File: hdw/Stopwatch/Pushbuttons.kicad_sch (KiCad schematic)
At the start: 42 parts

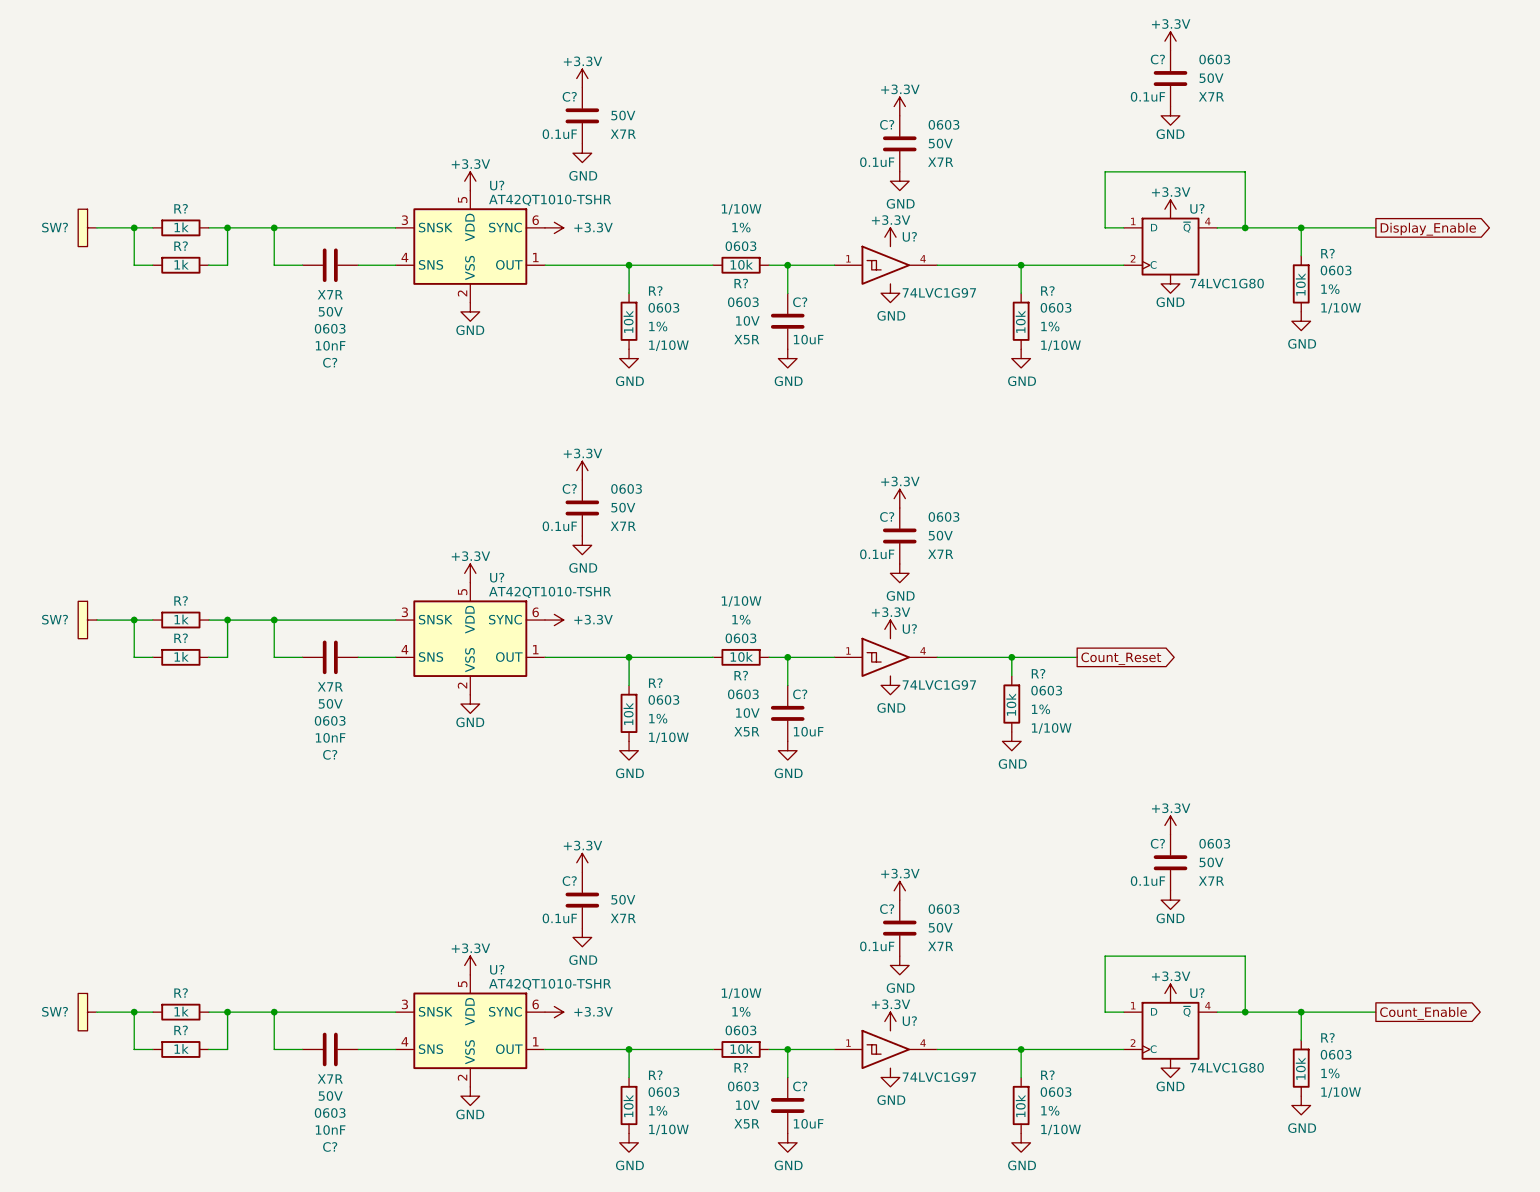
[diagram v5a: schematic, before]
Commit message: Assigned some digikey pns
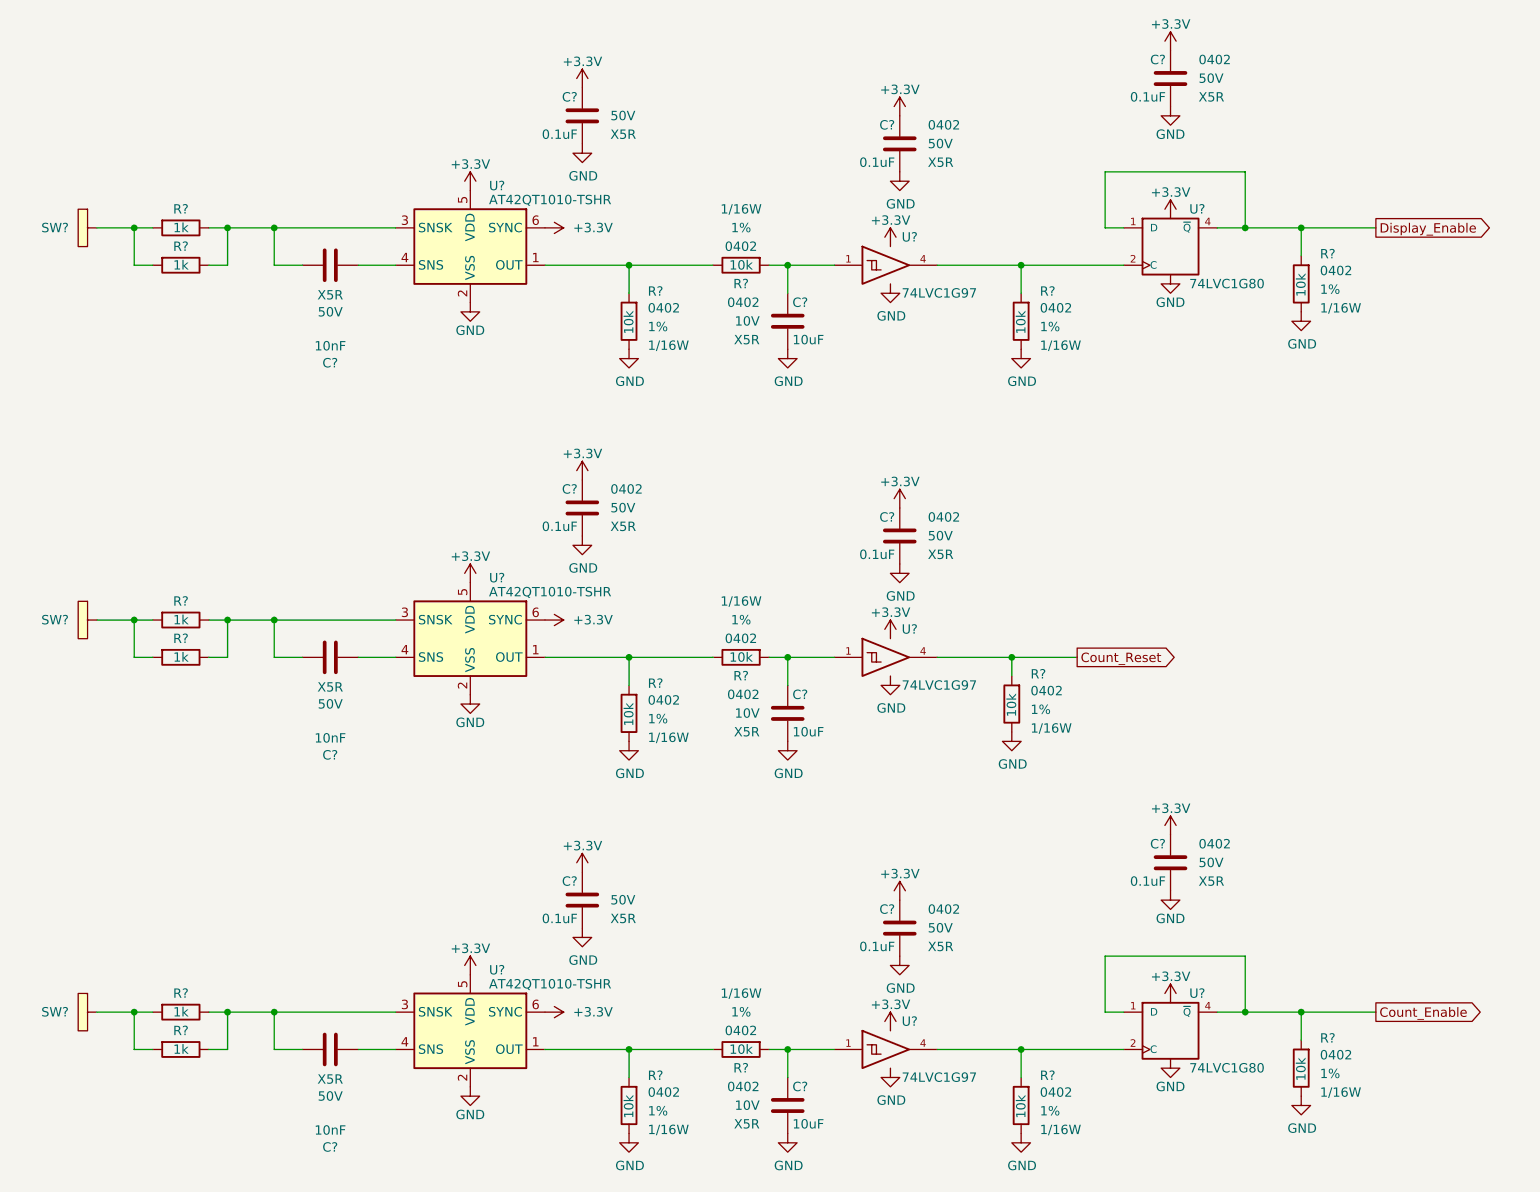
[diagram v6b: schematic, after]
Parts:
- C? (x3): footprint Capacitors_SMD:C_0603 -> Capacitors_SMD:C_0402; Dielectric X7R -> X5R; Digi-Key PN 1276-1921-1-ND -> 445-12201-1-ND; display_footprint 0603 -> (none)
- C? (x8): footprint Capacitors_SMD:C_0603 -> Capacitors_SMD:C_0402; Dielectric X7R -> X5R; Digi-Key PN 311-1344-1-ND -> 490-10697-1-ND; display_footprint 0603 -> 0402
- C? (x3): footprint Capacitors_SMD:C_0603 -> Capacitors_SMD:C_0402; Digi-Key PN 490-14372-1-ND -> 490-GRM155R61A106ME11DCT-ND; display_footprint 0603 -> 0402
- R? (x11): footprint Resistors_SMD:R_0603 -> Resistors_SMD:R_0402; Digi-Key PN RMCF0603FT10K0CT-ND -> RMCF0402FT10K0CT-ND; Wattage 1/10W -> 1/16W; display_footprint 0603 -> 0402
- R? (x6): footprint Resistors_SMD:R_0603 -> Resistors_SMD:R_0402; Digi-Key PN RHM1.0KDCT-ND -> RMCF0402FT1K00CT-ND; Wattage 1/10W -> 1/16W; display_footprint 0603 -> 0402
- U? (x2): footprint TO_SOT_Packages_SMD:SOT-353_SC-70-5 -> Package_SON:Texas_X2SON-5_0.8x0.8mm_P0.48mm; Digi-Key PN 296-9852-1-ND -> 1727-74LVC1G80GX,125CT-ND
- U? (x3): footprint Package_TO_SOT_SMD:SOT-363_SC-70-6 -> (none); Digi-Key PN (none) -> 296-29875-1-ND

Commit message: added proper power sequencing, discharge
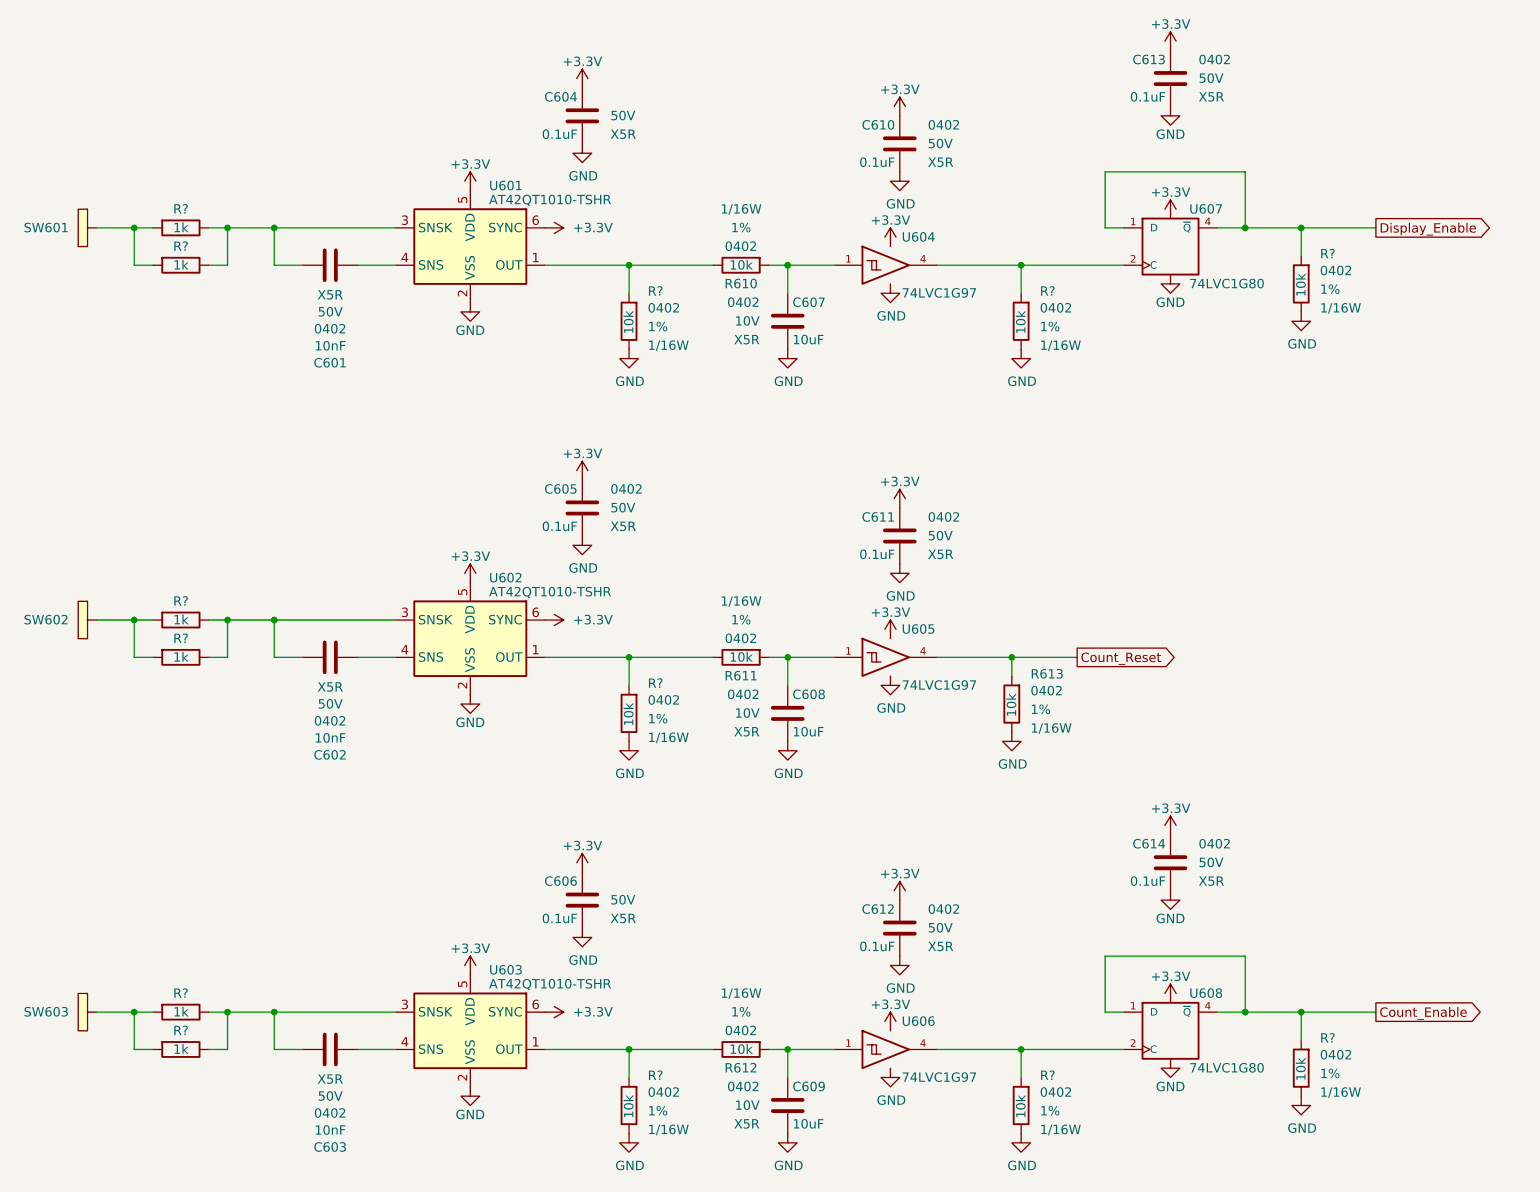
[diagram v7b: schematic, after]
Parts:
- C601, C602, C603: renamed from C?; display_footprint (none) -> 0402
- U604, U605, U606: renamed from U?; footprint (none) -> Package_SON:Fairchild_MicroPak2-6_1.0x1.0mm_P0.35mm
- gave numbers to parts that had none: 23

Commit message: lots and lots of routing
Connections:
- net +3V3 renamed +3.3V
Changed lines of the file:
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@@
     )
   )
-  (symbol (lib_id "Incrementor-rescue:+3.3V-power") (at 194.31 40.64 0) (unit 1)
+  (symbol (lib_id "power:+3.3V") (at 194.31 40.64 0) (unit 1)
     (in_bom yes) (on_board yes) (dnp no)
     (property "Reference" "#PWR0639" (at 194.31 44.45 0)
@@
     )
   )
-  (symbol (lib_id "Incrementor-rescue:+3.3V-power") (at 194.31 17.78 0) (unit 1)
+  (symbol (lib_id "power:+3.3V") (at 194.31 17.78 0) (unit 1)
     (in_bom yes) (on_board yes) (dnp no)
     (property "Reference" "#PWR0637" (at 194.31 21.59 0)
@@
     )
   )
-  (symbol (lib_id "Incrementor-rescue:+3.3V-power") (at 156.21 44.45 0) (unit 1)
+  (symbol (lib_id "power:+3.3V") (at 156.21 44.45 0) (unit 1)
     (in_bom yes) (on_board yes) (dnp no)
     (property "Reference" "#PWR0622" (at 156.21 48.26 0)
@@
     )
   )
-  (symbol (lib_id "Incrementor-rescue:+3.3V-power") (at 157.48 26.67 0) (unit 1)
+  (symbol (lib_id "power:+3.3V") (at 157.48 26.67 0) (unit 1)
     (in_bom yes) (on_board yes) (dnp no)
     (property "Reference" "#PWR0628" (at 157.48 30.48 0)
@@
     )
   )
-  (symbol (lib_id "Incrementor-rescue:+3.3V-power") (at 156.21 97.79 0) (unit 1)
+  (symbol (lib_id "power:+3.3V") (at 156.21 97.79 0) (unit 1)
     (in_bom yes) (on_board yes) (dnp no)
     (property "Reference" "#PWR0624" (at 156.21 101.6 0)
@@
     )
   )
-  (symbol (lib_id "Incrementor-rescue:+3.3V-power") (at 157.48 80.01 0) (unit 1)
+  (symbol (lib_id "power:+3.3V") (at 157.48 80.01 0) (unit 1)
     (in_bom yes) (on_board yes) (dnp no)
     (property "Reference" "#PWR0630" (at 157.48 83.82 0)
@@
     )
   )
-  (symbol (lib_id "Incrementor-rescue:+3.3V-power") (at 114.3 76.2 0) (unit 1)
+  (symbol (lib_id "power:+3.3V") (at 114.3 76.2 0) (unit 1)
     (in_bom yes) (on_board yes) (dnp no)
     (property "Reference" "#PWR0612" (at 114.3 80.01 0)
@@
     )
   )
-  (symbol (lib_id "Incrementor-rescue:+3.3V-power") (at 157.48 133.35 0) (unit 1)
+  (symbol (lib_id "power:+3.3V") (at 157.48 133.35 0) (unit 1)
     (in_bom yes) (on_board yes) (dnp no)
     (property "Reference" "#PWR0632" (at 157.48 137.16 0)
@@
     )
   )
-  (symbol (lib_id "Incrementor-rescue:+3.3V-power") (at 194.31 147.32 0) (unit 1)
+  (symbol (lib_id "power:+3.3V") (at 194.31 147.32 0) (unit 1)
     (in_bom yes) (on_board yes) (dnp no)
     (property "Reference" "#PWR0643" (at 194.31 151.13 0)
@@
     )
   )
-  (symbol (lib_id "Incrementor-rescue:+3.3V-power") (at 194.31 124.46 0) (unit 1)
+  (symbol (lib_id "power:+3.3V") (at 194.31 124.46 0) (unit 1)
     (in_bom yes) (on_board yes) (dnp no)
     (property "Reference" "#PWR0641" (at 194.31 128.27 0)
@@
     )
   )
-  (symbol (lib_id "Incrementor-rescue:+3.3V-power") (at 109.22 95.25 270) (unit 1)
+  (symbol (lib_id "power:+3.3V") (at 109.22 95.25 270) (unit 1)
     (in_bom yes) (on_board yes) (dnp no)
     (property "Reference" "#PWR0608" (at 105.41 95.25 0)
@@
     )
   )
-  (symbol (lib_id "Incrementor-rescue:+3.3V-power") (at 99.06 36.83 0) (unit 1)
+  (symbol (lib_id "power:+3.3V") (at 99.06 36.83 0) (unit 1)
     (in_bom yes) (on_board yes) (dnp no)
     (property "Reference" "#PWR0601" (at 99.06 40.64 0)
@@
     )
   )
-  (symbol (lib_id "Incrementor-rescue:+3.3V-power") (at 99.06 90.17 0) (unit 1)
+  (symbol (lib_id "power:+3.3V") (at 99.06 90.17 0) (unit 1)
     (in_bom yes) (on_board yes) (dnp no)
     (property "Reference" "#PWR0603" (at 99.06 93.98 0)
@@
     )
   )
-  (symbol (lib_id "Incrementor-rescue:+3.3V-power") (at 114.3 129.54 0) (unit 1)
+  (symbol (lib_id "power:+3.3V") (at 114.3 129.54 0) (unit 1)
     (in_bom yes) (on_board yes) (dnp no)
     (property "Reference" "#PWR0614" (at 114.3 133.35 0)
@@
     )
   )
-  (symbol (lib_id "Incrementor-rescue:+3.3V-power") (at 109.22 148.59 270) (unit 1)
+  (symbol (lib_id "power:+3.3V") (at 109.22 148.59 270) (unit 1)
     (in_bom yes) (on_board yes) (dnp no)
     (property "Reference" "#PWR0609" (at 105.41 148.59 0)
@@
     )
   )
-  (symbol (lib_id "Incrementor-rescue:+3.3V-power") (at 156.21 151.13 0) (unit 1)
+  (symbol (lib_id "power:+3.3V") (at 156.21 151.13 0) (unit 1)
     (in_bom yes) (on_board yes) (dnp no)
     (property "Reference" "#PWR0626" (at 156.21 154.94 0)
@@
     )
   )
-  (symbol (lib_id "Incrementor-rescue:+3.3V-power") (at 109.22 41.91 270) (unit 1)
+  (symbol (lib_id "power:+3.3V") (at 109.22 41.91 270) (unit 1)
     (in_bom yes) (on_board yes) (dnp no)
     (property "Reference" "#PWR0607" (at 105.41 41.91 0)
@@
     )
   )
-  (symbol (lib_id "Incrementor-rescue:+3.3V-power") (at 99.06 143.51 0) (unit 1)
+  (symbol (lib_id "power:+3.3V") (at 99.06 143.51 0) (unit 1)
     (in_bom yes) (on_board yes) (dnp no)
     (property "Reference" "#PWR0605" (at 99.06 147.32 0)
@@
     )
   )
-  (symbol (lib_id "Incrementor-rescue:+3.3V-power") (at 114.3 22.86 0) (unit 1)
+  (symbol (lib_id "power:+3.3V") (at 114.3 22.86 0) (unit 1)
     (in_bom yes) (on_board yes) (dnp no)
     (property "Reference" "#PWR0610" (at 114.3 26.67 0)
